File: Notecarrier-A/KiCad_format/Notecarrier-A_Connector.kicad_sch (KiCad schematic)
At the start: 48 parts, among them J13 BM04B-SRSS-TBT, J14 BM04B-SRSS-TBT, J20 MDT420E01001, J5 NanoSIM - SF72S006VBAR2500, J7 uFL-R-SMT-1-10, J8 uFL-R-SMT-1-10, Q2 AO3420, U5 BGA725L6E6327FTSA1

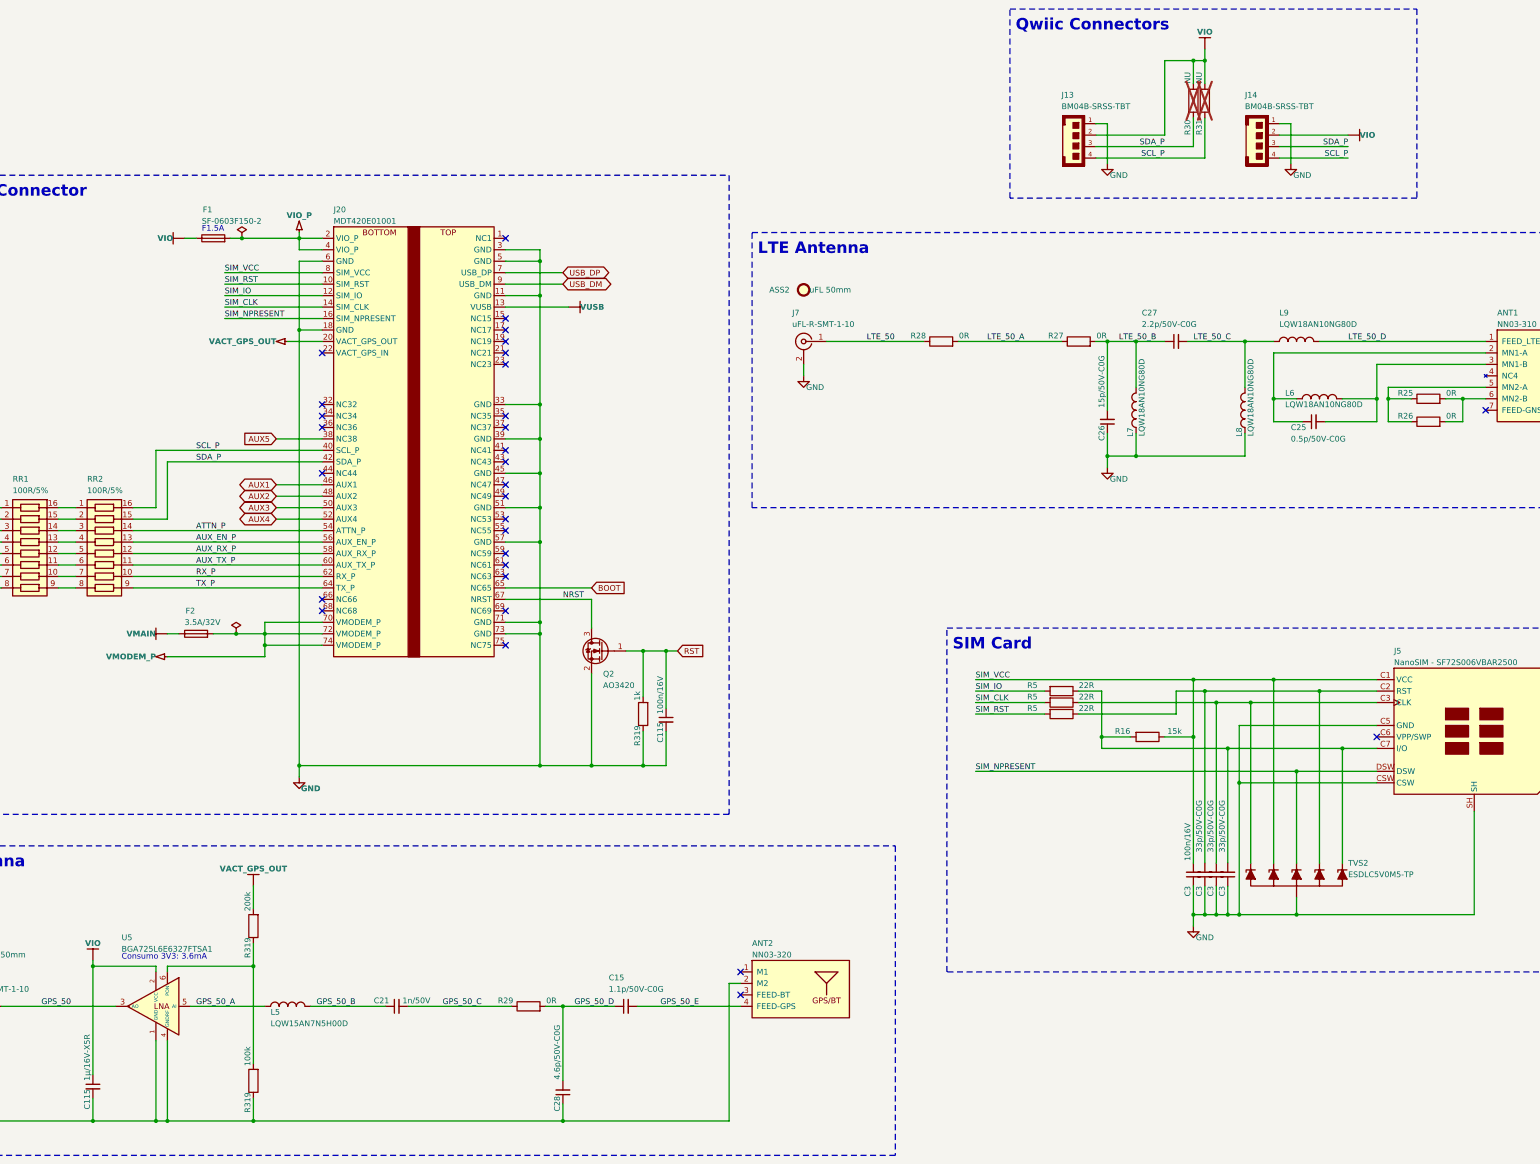
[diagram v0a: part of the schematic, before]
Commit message: Establish port of Notecarrier-B PCB.
Ported: components, board outline, fabrication layers, silkscreens and front copper.
To go: inner and back copper layers, drills, sheet metadata.
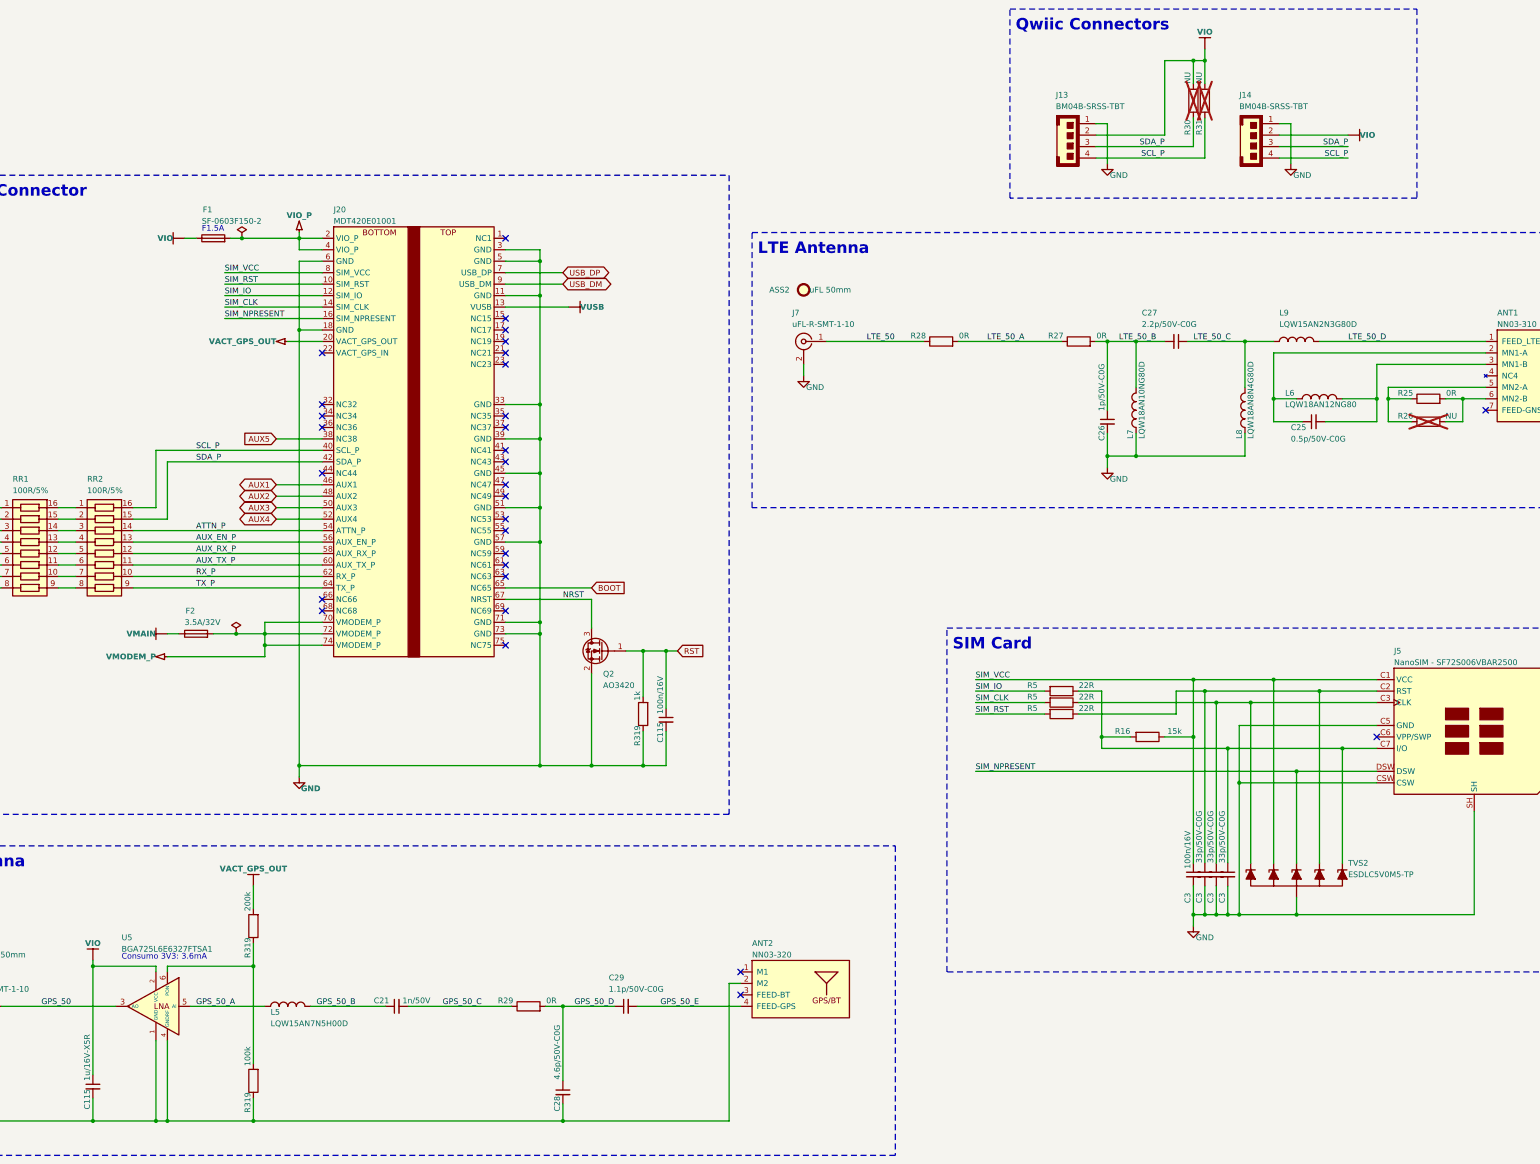
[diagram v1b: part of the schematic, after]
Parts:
- ANT1: footprint (none) -> blues-kicad-lib:ANT-NN03310-LTE_NO-SILK; Caratteristiche (none) -> LTE; Distributor (none) -> FAE; MPN (none) -> NN03-310; Note (none) -> 698MHz-960MHz - 1.71GHz-2.69GHz; Pkg Type (none) -> SMD; Temperature (none) -> -40°..+125°
- ANT2: footprint (none) -> blues-kicad-lib:ANT-NN03320-GPS_NO-SILK; Caratteristiche (none) -> GPS/GLONASS - BT; Distributor (none) -> FAE; MPN (none) -> NN03-320; Pkg Type (none) -> SMD; Temperature (none) -> -40°..+85°
- ASS2, ASS3: Distributor (none) -> FAE; Pkg Type (none) -> THT
- C115: value 1µ/16V-X5R -> 1u/16V-X5R; Caratteristiche (none) -> X5R; Distributor (none) -> FAE
- C115: Caratteristiche (none) -> X7R; Distributor (none) -> FAE
- C21: footprint (none) -> blues-kicad-lib:FRACTUS-0404_NO-SILK; Caratteristiche (none) -> X7R; Distributor (none) -> FAE; Pkg Type (none) -> SMD
- C25: footprint (none) -> blues-kicad-lib:FRACTUS-0404_NO-SILK; Caratteristiche (none) -> C0G; Distributor (none) -> FAE; MPN (none) -> GJM1555C1HR50WB01; Pkg Type (none) -> SMD; Temperature (none) -> -55°..+125°
- C26: value 15p/50V-C0G -> 1p/50V-C0G; footprint (none) -> blues-kicad-lib:FRACTUS-0404_NO-SILK; Caratteristiche (none) -> C0G; Distributor (none) -> FAE; MPN (none) -> GJM1555C1H1R0WB01; Pkg Type (none) -> SMD; Temperature (none) -> -55°..+125°
- C27: footprint (none) -> blues-kicad-lib:FRACTUS-0404_NO-SILK; Caratteristiche (none) -> C0G; Distributor (none) -> FAE; MPN (none) -> GJM1555C1H2R2WB01; Pkg Type (none) -> SMD; Temperature (none) -> -55°..+125°
- C28: footprint (none) -> blues-kicad-lib:FRACTUS-0404_NO-SILK; Caratteristiche (none) -> C0G; Distributor (none) -> M-81-GJM1555C1H4R6WB1D; MPN (none) -> GJM1555C1H4R6WB01D; Note (none) -> RF; Pkg Type (none) -> SMD; Temperature (none) -> -55°..+125°
- C29: renamed from C15; footprint (none) -> blues-kicad-lib:FRACTUS-0404_NO-SILK; Caratteristiche (none) -> C0G; Distributor (none) -> D-490-11194-1-ND; MPN (none) -> GJM1555C1H1R1WB01D; Note (none) -> RF; Pkg Type (none) -> SMD; Temperature (none) -> -55°..+125°
- C3: footprint blues-kicad-lib:CAP 0402_1005 -> blues-kicad-lib:CS-C-0402; Caratteristiche (none) -> C0G; Distributor (none) -> FAE; Manufacturer Samsung -> (none); Order Code 1276-1272-1-ND -> (none); Part Number CL05C330JB5NNNC -> (none); Pkg Type (none) -> SMD; Supplier Digi-Key -> (none)
- C3: footprint blues-kicad-lib:CAP 0402_1005 -> blues-kicad-lib:CS-C-0402; Caratteristiche (none) -> X7R; Distributor (none) -> FAE; Manufacturer Samsung -> (none); Order Code 187-CL05B104KO5NNNC -> (none); Part Number CL05B104KO5NNNC -> (none); Pkg Type (none) -> SMD; Supplier Farnell -> (none)
- F1: Caratteristiche (none) -> 1.5A/32V; Distributor (none) -> FAE
- F2: Caratteristiche (none) -> 3.5A/32V; Distributor (none) -> FAE
- J13, J14: footprint (none) -> blues-kicad-lib:J-4-0100-MDS-SH_NO-SILK; Caratteristiche (none) -> 4P; Distributor (none) -> D-455-2874-1-ND; MPN (none) -> BM04B-SRSS-TBT(LF)(SN); Manufacturer JST -> (none); Pkg Type (none) -> SMD; Temperature (none) -> -25°..+85°
- J20: Caratteristiche (none) -> 75P; Distributor (none) -> FAE
- J5: footprint blues-kicad-lib:J-NANOSIM-SF72S006VBA -> blues-kicad-lib:J-NANOSIM-SF72S006VBA_NO-FILL; Distributor (none) -> FAE; MPN (none) -> SF72S006VBAR2500; Manufacturer JAE Electronics -> (none); Order Code 670-2967-1-ND -> (none); Part Number SF72S006VBDR2500 -> (none); Pkg Type (none) -> SMD; Supplier Digi-Key -> (none); Temperature (none) -> -25°..+85°
- J7, J8: footprint (none) -> blues-kicad-lib:J-3-MDS-UFL_NO-SILK; Caratteristiche (none) -> RF; Distributor (none) -> FAE; MPN (none) -> U.FL-R-SMT-1(10); Note (none) -> 50ohm; Pkg Type (none) -> SMD; Temperature (none) -> -40°..+90°
- L5: footprint (none) -> blues-kicad-lib:FRACTUS-0404_NO-SILK; Caratteristiche (none) -> 570mA; Distributor (none) -> FAE; MPN (none) -> LQW15AN7N5H00D; Note (none) -> Non Schermato - 6GHz; Pkg Type (none) -> SMD; Temperature (none) -> -55°..+125°
- L6: value LQW18AN10NG80D -> LQW18AN12NG80; footprint (none) -> blues-kicad-lib:FRACTUS-0404_NO-SILK; Caratteristiche (none) -> 1.5A; Distributor (none) -> FAE; MPN (none) -> LQW18AN12NG80; Pkg Type (none) -> SMD; Temperature (none) -> -55°..+125°
- L7: footprint (none) -> blues-kicad-lib:FRACTUS-0404_NO-SILK; Caratteristiche (none) -> 1.6A; Distributor (none) -> FAE; MPN (none) -> LQW18AN10NG80D; Pkg Type (none) -> SMD; Temperature (none) -> -55°..+125°
- L8: value LQW18AN10NG80D -> LQW18AN8N4G80D; footprint (none) -> blues-kicad-lib:FRACTUS-0404_NO-SILK; Caratteristiche (none) -> 1.6A; Distributor (none) -> FAE; MPN (none) -> LQW18AN8N4G80D; Pkg Type (none) -> SMD; Temperature (none) -> -55°..+125°
- L9: value LQW18AN10NG80D -> LQW15AN2N3G80D; footprint (none) -> blues-kicad-lib:FRACTUS-0404_NO-SILK; Caratteristiche (none) -> 2.53A; Distributor (none) -> FAE; MPN (none) -> LQW15AN2N3G80D; Pkg Type (none) -> SMD; Temperature (none) -> -55°..+125°
- Q2: Caratteristiche (none) -> 6A(Ta)/20V; Distributor (none) -> FAE; Note (none) -> Vth=0.75V - Rdson=25mohm
- R16: footprint blues-kicad-lib:RES 0402_1005 -> blues-kicad-lib:RS-0402; Caratteristiche (none) -> 1%; Distributor (none) -> FAE; Manufacturer Cyntec -> (none); Order Code 2037-PFR05S-153-FNHCT-ND -> (none); Part Number PFR05S-153-FNH -> (none); Pkg Type (none) -> SMD; Supplier Digi-Key -> (none); Temperature (none) -> -55°..+155°
- R25, R27, R28, R29: footprint (none) -> blues-kicad-lib:FRACTUS-0404_NO-SILK; Caratteristiche (none) -> 1%; Distributor (none) -> FAE; Pkg Type (none) -> SMD; Temperature (none) -> -55°..+150°
- R26: value 0R -> NU; footprint (none) -> blues-kicad-lib:FRACTUS-0404_NO-SILK; Pkg Type (none) -> SMD; now not fitted
- R30, R31: footprint (none) -> blues-kicad-lib:RS-0603; Pkg Type (none) -> SMD
- R319: Caratteristiche (none) -> 1%; Distributor (none) -> FAE; Temperature -55°..+155° -> (none)
- R319: Caratteristiche (none) -> 1%; Distributor (none) -> FAE
- R5: footprint blues-kicad-lib:RES 0402_1005 -> blues-kicad-lib:RS-0603; Caratteristiche (none) -> 1%; Distributor (none) -> FAE; Manufacturer Yageo -> (none); Order Code 311-22.0LRCT-ND -> (none); Part Number RC0402FR-0722RL -> (none); Pkg Type (none) -> SMD; Supplier Digi-Key -> (none)
- RR1, RR2: footprint blues-kicad-lib:RESNET 1506-16 CONVEX -> blues-kicad-lib:RR-8X-1506; Caratteristiche (none) -> 8X; Distributor (none) -> FAE; Manufacturer CTS -> (none); Note (none) -> 200ppm; Order Code 741X163101JPCT-ND -> (none); Part Number 741X163101JP -> (none); Pkg Type (none) -> SMD; Supplier Digi-Key -> (none); Temperature (none) -> -55°..+125°
- TVS2: footprint blues-kicad-lib:SOT666 -> blues-kicad-lib:SOT666_NO-SILK; Caratteristiche (none) -> 1.6A/5V/20W; Distributor (none) -> FAE; Manufacturer Nexperia -> (none); Note (none) -> Cmax=10pF - SIM; Order Code 1727-5797-1-ND -> (none); Part Number PESD5V0L5UV125 -> (none); Pkg Type (none) -> SMD; Supplier Digi-Key -> (none); Temperature (none) -> -65°..+150°
- U5: footprint (none) -> blues-kicad-lib:XFDFN6_NO-SILK; Caratteristiche (none) -> RF; Distributor (none) -> FAE; MPN (none) -> BGA725L6E6327FTSA1; Note (none) -> VCC=1.5V - 3.6V; Pkg Type (none) -> SMD; Temperature (none) -> -40°..+125°
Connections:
- net GND: now also C26.2, C28.2, C3.2, C3.2, C3.2, C3.2, L7.2, L8.2; no longer C26.1, C28.1, C3.1, C3.1, C3.1, C3.1, L7.1, L8.1
- net GPS_50_D: now also C28.1; no longer C28.2
- net LTE_50_B: now also C26.1, C27.2, L7.1; no longer C26.2, C27.1, L7.2
- net LTE_50_C: now also C27.1, L8.1; no longer C27.2, L8.2
- net SIM_VCC: now also C3.1; no longer C3.2
- net at J5.C3 (CLK), R5.1, TVS2.1 (K1): now also C3.1; no longer C3.2
- net at J5.C2 (RST), R5.1, TVS2.5 (K4): now also C3.1; no longer C3.2
- net at J5.C7 (I/O), R16.2, R5.1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: now also C3.1; no longer C3.2
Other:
- moved on the sheet: C26, C27, C28, C3, J13, J14, L7, L8
